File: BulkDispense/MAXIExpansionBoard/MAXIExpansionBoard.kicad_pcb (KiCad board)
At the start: 2 copper layers, 57.2 x 100 mm, 30 parts, among them J1 BS1~4, J10 FS3, J11 R6~R7, J12 R8~R9, J13 OS1~4, J14 WV1~2, J15 FS2, J16 FS4, J17 Analog Inputs, J18 Digital IN + R0~R4, J19 Digital Outputs, J2 MV1~4, J20 R4~R9, J21 Flow Sensors, J3 WB/WL, J4 PS/PCV, J5 Screw_Terminal_01x02, J6 R0~R1, J7 R2~R3, J8 R4~R5, J9 FS1

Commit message: Design Overhaul
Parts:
- removed kibuzzard-684C282C: G***, kibuzzard-684C282C
- removed kibuzzard-684C2929: G***, kibuzzard-684C2929
- removed kibuzzard-684C293C: G***, kibuzzard-684C293C
- removed kibuzzard-684C2942: G***, kibuzzard-684C2942
- removed kibuzzard-684C2947: G***, kibuzzard-684C2947
- added H10: MountingHole, MountingHole:MountingHole_2.5mm, F.Cu at (200.6, 84.4)
- added H11: MountingHole, MountingHole:MountingHole_3.2mm_M3, F.Cu at (125.2, 42.7)
- added H5: MountingHole, MountingHole:MountingHole_2.5mm, F.Cu at (213.3, 104.7)
- added H6: MountingHole, MountingHole:MountingHole_2.5mm, F.Cu at (200.6, 104.7)
- added H7: MountingHole, MountingHole:MountingHole_2.5mm, F.Cu at (213.3, 120.0)
- added H8: MountingHole, MountingHole:MountingHole_2.5mm, F.Cu at (213.3, 135.3)
- added H9: MountingHole, MountingHole:MountingHole_2.5mm, F.Cu at (213.3, 84.4)
- added J22: OS1~4, PartsLibrary:CONN_37204-62A3-004PL_3MM, F.Cu at (182.4, 76.4)
- added J23: WB-MV5~6, PartsLibrary:CONN_37204-62A3-004PL_3MM, F.Cu at (163.0, 76.5)
- H1, H2, H3, H4: footprint MountingHole:MountingHole_2.2mm_M2 -> MountingHole:MountingHole_3.2mm_M3
- J1: value BS1~4 -> R0~R5; footprint PartsLibrary:CONN_37204-62A3-004PL_3MM -> PartsLibrary:CONN_37212-62M3-003PL_3MM
- J10: value FS3 -> FS2~FS4; footprint PartsLibrary:CONN_37204-62A3-004PL_3MM -> PartsLibrary:CONN_37212-62M3-003PL_3MM
- J11: value R6~R7 -> MV1~4
- J12: value R8~R9 -> WB/WL
- J13: value OS1~4 -> PS/PCV; footprint PartsLibrary:CONN_37204-62A3-004PL_3MM -> PartsLibrary:3720362A3003PL
- J14: value WV1~2 -> RV1&2; footprint PartsLibrary:3720362A3003PL -> PartsLibrary:CONN_37204-62A3-004PL_3MM
- J15: value FS2 -> RV3&4
- J16: value FS4 -> FS1
- J17: value Analog Inputs -> FS3; footprint PartsLibrary:CONN_37212-62M3-003PL_3MM -> PartsLibrary:CONN_37204-62A3-004PL_3MM
- J18: value Digital IN + R0~R4 -> WB-MV1~4; footprint PartsLibrary:CONN_37212-62M3-003PL_3MM -> PartsLibrary:CONN_37204-62A3-004PL_3MM
- J19: value Digital Outputs -> FS2; footprint PartsLibrary:CONN_37212-62M3-003PL_3MM -> PartsLibrary:CONN_37204-62A3-004PL_3MM
- J2: value MV1~4 -> BS1~4; footprint PartsLibrary:CONN_37204-62A3-004PL_3MM -> PartsLibrary:CONN_37212-62M3-003PL_3MM
- J20: value R4~R9 -> FS4; footprint PartsLibrary:CONN_37212-62M3-003PL_3MM -> PartsLibrary:CONN_37204-62A3-004PL_3MM
- J21: value Flow Sensors -> BS1~4; footprint PartsLibrary:CONN_37212-62M3-003PL_3MM -> PartsLibrary:CONN_37204-62A3-004PL_3MM
- J3: value WB/WL -> Screw_Terminal_01x02; footprint PartsLibrary:CONN_37204-62A3-004PL_3MM -> PartsLibrary:691137710002
- J4: value PS/PCV -> DigitalOUT 0~3; footprint PartsLibrary:3720362A3003PL -> PartsLibrary:CONN_37204-62A3-004PL_3MM
- J5: value Screw_Terminal_01x02 -> DigitalOUT 4~7; footprint PartsLibrary:691137710002 -> PartsLibrary:CONN_37204-62A3-004PL_3MM
- J6: value R0~R1 -> OS1~4; footprint PartsLibrary:CONN_37204-62A3-004PL_3MM -> PartsLibrary:CONN_37212-62M3-003PL_3MM
- J7: value R2~R3 -> AnalogIOs; footprint PartsLibrary:CONN_37204-62A3-004PL_3MM -> PartsLibrary:CONN_37212-62M3-003PL_3MM
- J8: value R4~R5 -> Fan PWR; footprint PartsLibrary:CONN_37204-62A3-004PL_3MM -> PartsLibrary:3720362A3003PL
- moved J3 85.5 mm to (136.8, 47.1), turned to 180 degrees
- moved J1 79.3 mm to (130.0, 62.3), turned to 0 degrees
- moved J19 77.5 mm to (163.9, 126.7)
- moved J8 70.9 mm to (204.7, 47.1), turned to 0 degrees
- moved H1 68.1 mm to (172.8, 90.2)
- moved J6 65.3 mm to (174.6, 46.8), turned to 0 degrees
- moved J12 63.1 mm to (182.4, 69.0), turned to 0 degrees
- moved J4 57.3 mm to (130.1, 98.2), turned to 90 degrees
- moved J18 56.5 mm to (186.0, 94.8)
- moved J21 53.4 mm to (182.4, 61.6)
- moved J11 51.0 mm to (186.0, 87.3), turned to 0 degrees
- moved J5 50.9 mm to (137.7, 98.2), turned to 90 degrees
- moved H4 42.7 mm to (220.2, 137.7)
- moved H3 42.7 mm to (220.2, 42.8)
- moved J9 39.1 mm to (145.3, 98.3)
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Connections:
- J1 pad 1: /AI0 -> /R0_IN
- J1 pad 2: /AI1 -> /R1_IN
- J1 pad 3: /AI2 -> /R2_IN
- J1 pad 4: /AI3 -> /R3_IN
- J1 pad 5: (no net) -> /R4_IN
- J1 pad 6: (no net) -> /R5_IN
- J10 pad 1: /FS3-1 -> /FS2-1
- J10 pad 2: /FS3-2 -> /FS2-2
- J10 pad 3: /FS3-3 -> /FS2-3
- J10 pad 4: /FS3-4 -> /FS2-4
- J10 pad 5: (no net) -> /FS3-1
- J10 pad 6: (no net) -> /FS3-2
- J11 pad 1: /R6_OUT -> /DO0
- J11 pad 2: /R6_IN -> /DO1
- J11 pad 3: /R7_OUT -> /DO2
- J11 pad 4: /R7_IN -> /DO3
- J12 pad 1: /R8_OUT -> /AI4
- J12 pad 2: /R8_IN -> /AI5
- J12 pad 3: /R9_OUT -> /AI6
- J12 pad 4: /R9_IN -> /AI7
- J13 pad 1: /DI0 -> /AI12
- J13 pad 2: /DI1 -> /AI13
- J13 pad 3: /DI2 -> /AO0
- J14 pad 1: /AI8 -> /R0_OUT
- J14 pad 2: /AI9 -> /R0_IN
- J14 pad 3: unconnected-(J14-Pin_3-Pad3) -> /R1_OUT
- J15 pad 1: /FS2-1 -> /R2_OUT
- J15 pad 2: /FS2-2 -> /R2_IN
- J15 pad 3: /FS2-3 -> /R3_OUT
- J15 pad 4: /FS2-4 -> /R3_IN
- J16 pad 1: /FS4-1 -> /FS1-1
- J16 pad 2: /FS4-2 -> /FS1-2
- J16 pad 3: /FS4-3 -> /FS1-3
- J16 pad 4: /FS4-4 -> /FS1-4
- J17 pad 1: /AI0 -> /FS3-1
- J17 pad 2: /AI1 -> /FS3-2
- J17 pad 3: /AI2 -> /FS3-3
- J17 pad 4: /AI3 -> /FS3-4
- J17 pad 5: /AI4 -> (no net)
- J17 pad 6: /AI5 -> (no net)
- J18 pad 1: /DI0 -> /DO4
- J18 pad 2: /DI1 -> /DO5
- J18 pad 3: /DI2 -> /DO6
- J18 pad 4: /DI3 -> /DO7
- J18 pad 5: /R0_IN -> (no net)
- J18 pad 6: /R1_IN -> (no net)
- J19 pad 1: +24V -> /FS2-1
- J19 pad 2: GND -> /FS2-2
- J19 pad 3: /AI12 -> /FS2-3
- J19 pad 4: /AI13 -> /FS2-4
- J19 pad 5: /DO0 -> (no net)
- J19 pad 6: /DO1 -> (no net)
- J2 pad 1: /DO0 -> +24V
- J2 pad 2: /DO1 -> GND
- J2 pad 3: /DO2 -> /AI0
- J2 pad 4: /DO3 -> +24V
- J2 pad 5: (no net) -> GND
- J2 pad 6: (no net) -> /AI1
- J20 pad 1: /R4_IN -> /FS4-1
- J20 pad 2: /R5_IN -> /FS4-2
- J20 pad 3: /R6_IN -> /FS4-3
- J20 pad 4: /R7_IN -> /FS4-4
- J20 pad 5: /R8_IN -> (no net)
- J20 pad 6: /R9_IN -> (no net)
- J21 pad 1: /FS2-3 -> /AI0
- J21 pad 2: /FS2-4 -> /AI1
- J21 pad 3: /FS3-1 -> /AI2
- J21 pad 4: /FS3-2 -> /AI3
- J21 pad 5: /FS3-3 -> (no net)
- J21 pad 6: /FS3-4 -> (no net)
- J3 pad 1: /AI4 -> +24V
- J3 pad 2: /AI5 -> GND
- J4 pad 1: /AI12 -> /DO0
- J4 pad 2: /AI13 -> /DO1
- J4 pad 3: /AO0 -> /DO2
- J5 pad 1: +24V -> /DO4
- J5 pad 2: GND -> /DO5
- J6 pad 1: /R0_OUT -> +24V
- J6 pad 2: /R0_IN -> GND
- J6 pad 3: /R1_OUT -> /DI0
- J6 pad 4: /R1_IN -> +24V
- J6 pad 5: (no net) -> GND
- J6 pad 6: (no net) -> /DI1
- J7 pad 1: /R2_OUT -> /AI4
- J7 pad 2: /R2_IN -> /AI5
- J7 pad 3: /R3_OUT -> /AI6
- J7 pad 4: /R3_IN -> /AI7
- J7 pad 5: (no net) -> /AI12
- J7 pad 6: (no net) -> /AI13
- J8 pad 1: /R4_OUT -> +24V
- J8 pad 2: /R4_IN -> /R6_OUT
- J8 pad 3: /R5_OUT -> unconnected-(J8-Pin_3-Pad3)
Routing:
- net +24V: track 12.8 -> 132.0 mm
- net /AI8: track 84.7 -> 0.00 mm, vias 2 -> 0
- net /AI9: track 74.8 -> 0.00 mm, vias 1 -> 0
- net /AI6: track 31.8 -> 102.3 mm, vias 0 -> 1
- net /AI5: track 32.6 -> 99.9 mm, vias 0 -> 1
- net /AI4: track 32.1 -> 96.0 mm, vias 0 -> 1
- net /DO7: track 0.00 -> 58.8 mm
- net /DO5: track 0.00 -> 56.8 mm
- net /DO6: track 0.00 -> 56.6 mm
- net /FS2-4: track 31.0 -> 83.9 mm, vias 0 -> 1
- net /DO4: track 0.00 -> 50.6 mm
- net /FS2-2: track 32.3 -> 80.9 mm
- net /AI7: track 34.7 -> 81.1 mm
- net /FS2-1: track 34.3 -> 78.3 mm, vias 0 -> 1
- net /FS2-3: track 35.9 -> 79.1 mm
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- added copper zone on B.Cu, net GND
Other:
- board size 57.2 x 100 mm -> 100 x 100 mm
- board text added: "I2C Bus"
- board text added: "I2C Hot Swap"

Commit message: Add latest design
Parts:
- added H10: MountingHole, MountingHole:MountingHole_2.5mm, F.Cu at (223.5, 85.1)
- added H5: MountingHole, MountingHole:MountingHole_2.5mm, F.Cu at (210.8, 64.7)
- added H6: MountingHole, MountingHole:MountingHole_2.5mm, F.Cu at (223.5, 64.7)
- added H9: MountingHole, MountingHole:MountingHole_2.5mm, F.Cu at (210.8, 85.1)
- added J24: LDS, PartsLibrary:CONN_37204-62A3-004PL_3MM, F.Cu at (187.4, 77.7)
- J13, J8: footprint PartsLibrary:3720362A3003PL -> PartsLibrary:CONN_37203-62A3-003PL_3MM
- moved H13 57.1 mm to (257.7, 84.7), turned to 90 degrees
- moved H15 46.3 mm to (257.7, 97.4), turned to 90 degrees
- moved H12 41.8 mm to (237.3, 84.7), turned to 90 degrees
- moved H3 38.9 mm to (259.1, 43.9)
- moved H4 38.8 mm to (259.0, 136.8)
- moved H8 37.0 mm to (225.0, 100.3), turned to -90 degrees
- moved J23 35.3 mm to (187.5, 101.9)
- moved H1 30.8 mm to (203.6, 91.2)
- moved H14 25.1 mm to (237.3, 97.4), turned to 90 degrees
- moved J19 25.1 mm to (187.4, 118.0)
- moved J17 24.6 mm to (187.4, 126.0)
- moved J16 23.7 mm to (187.4, 109.9)
- moved J20 23.5 mm to (187.4, 134.1)
- moved J11 21.6 mm to (166.5, 77.9)
- moved H7 20.1 mm to (209.6, 100.2), turned to -90 degrees
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- renumbered H6 to H12, H10 to H13, H5 to H14, H9 to H15
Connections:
- J7 pad 10: +24V -> /LDS
- J7 pad 11: unconnected-(J7-Pin_11-Pad11) -> +24V
- J7 pad 7: unconnected-(J7-Pin_7-Pad7) -> /AO0
- J7 pad 8: /AO0 -> /LDS-5V
- J7 pad 9: unconnected-(J7-Pin_9-Pad9) -> /LDS-GND
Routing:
- net GND: track 0.00 -> 122.6 mm
- net +24V: track 132.0 -> 220.9 mm
- net /LDS: track 0.00 -> 79.4 mm, vias 0 -> 1
- net /LDS-GND: track 0.00 -> 76.9 mm, vias 0 -> 1
- net /LDS-5V: track 0.00 -> 71.0 mm, vias 0 -> 1
- net /R4_OUT: track 18.5 -> 67.4 mm, vias 0 -> 1
- net /R4_IN: track 36.7 -> 80.0 mm
- net /R5_OUT: track 25.6 -> 67.2 mm
- net /R5_IN: track 39.0 -> 76.1 mm
- net /FS4-1: track 61.7 -> 88.9 mm, vias 0 -> 1
- net /FS3-4: track 61.6 -> 85.8 mm
- net /AI12: track 32.4 -> 54.9 mm, vias 0 -> 1
- net /FS3-1: track 62.5 -> 84.1 mm
- net /FS4-2: track 63.7 -> 84.6 mm, vias 0 -> 1
- net /AI5: track 99.9 -> 82.4 mm
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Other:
- board size 100 x 100 mm -> 139.7 x 100 mm
- board text added: "BS1 BS2"
- board text added: "BS1~4"
- board text added: "BS3 BS4"
- board text added: "FS1"
- board text added: "FS2"
- board text added: "FS3"
- board text added: "FS4"
- board text added: "Fan PWR"
- board text added: "LEAK"
- board text added: "MV1 MV2"
- board text added: "MV3 MV4"
- board text added: "MV5 MV6"
- board text added: "OS1 OS2"
- board text added: "OS1~4"
- board text added: "OS3 OS4"
- board text added: "PORT1 R0~R5"
- board text added: "PORT2 FS2~ FS4"
- board text added: "PORT3 DO FS1"
- board text added: "PORT4 AIO"
- board text added: "PS PCV"
- board text added: "RV1 RV2"
- board text added: "RV3 RV4"
- board text added: "Temp/Humidity Sensor"
- board text added: "WB"
- board text added: "WB MV1~4"
- board text added: "WB WL"

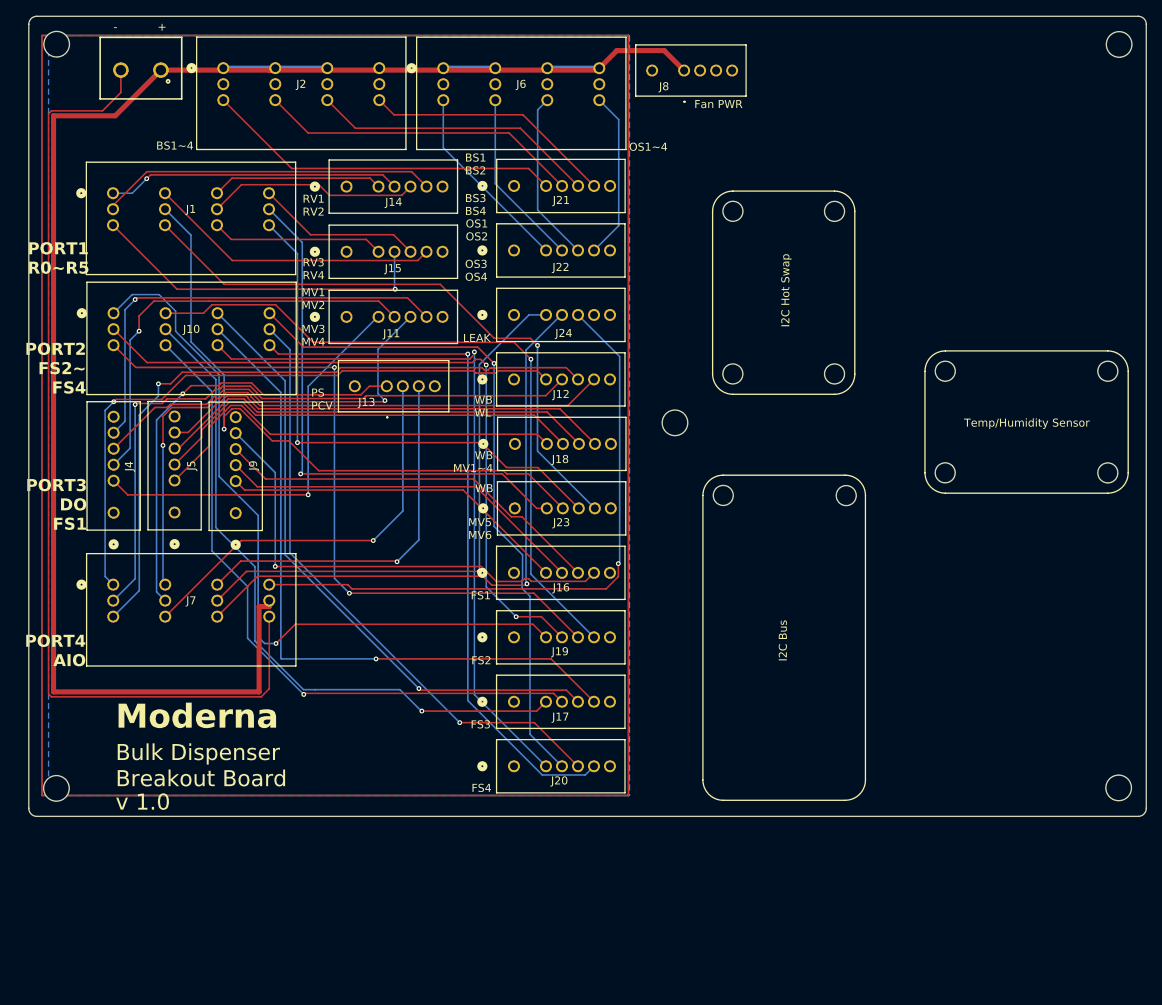
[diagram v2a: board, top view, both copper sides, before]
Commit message: Update PCB + Add Lynx Wiring Diagram
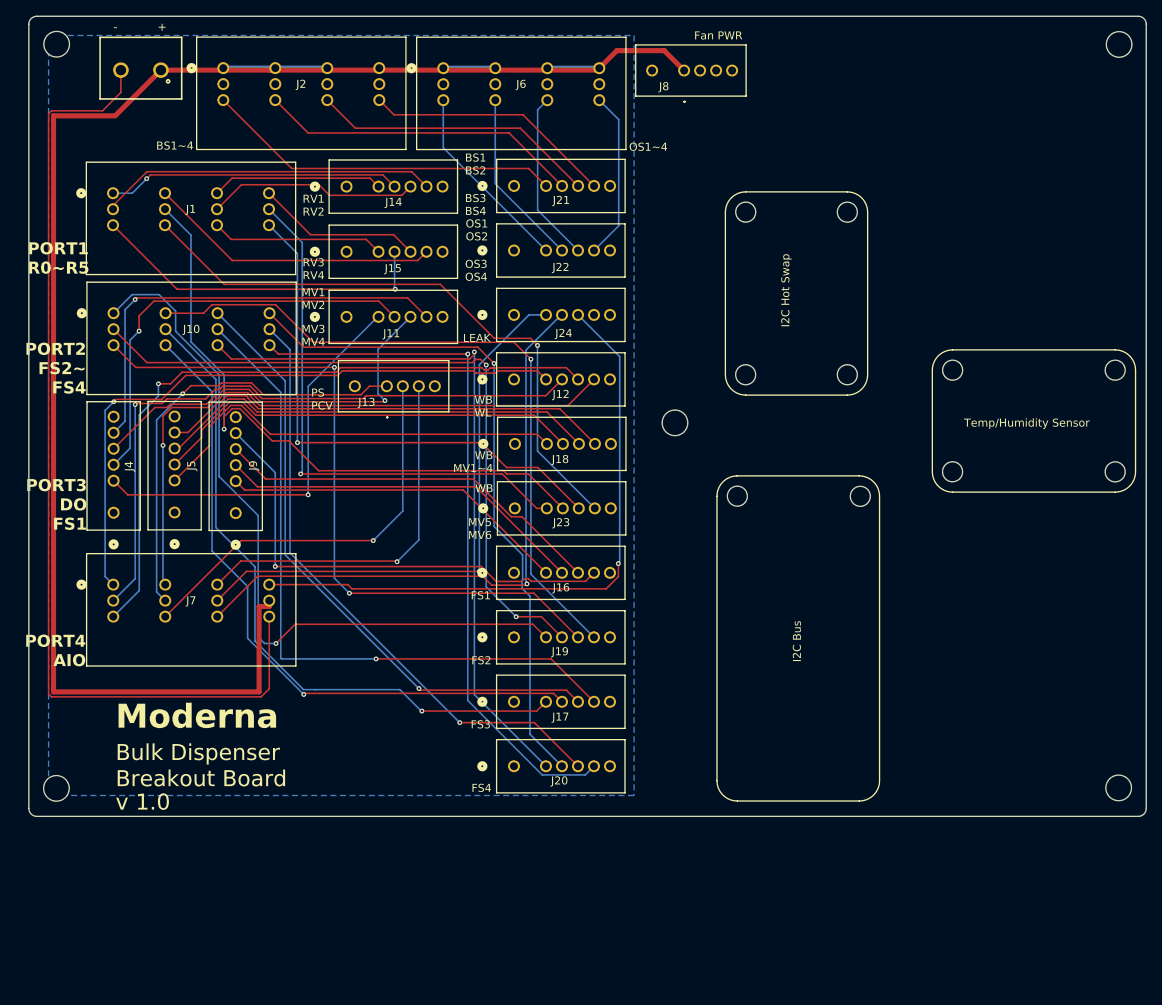
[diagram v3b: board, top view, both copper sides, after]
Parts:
- moved H8 1.76 mm to (226.7, 100.4)
- moved H7 1.76 mm to (211.3, 100.3)
- moved H9 1.60 mm to (212.4, 85.2)
- moved H6 1.60 mm to (225.1, 64.8)
- moved H10 1.60 mm to (225.1, 85.2)
- moved H5 1.60 mm to (212.4, 64.8)
- moved H15 0.93 mm to (258.6, 97.3)
- moved H12 0.93 mm to (238.3, 84.6)
- moved H13 0.93 mm to (258.6, 84.6)
- moved H14 0.93 mm to (238.2, 97.3)
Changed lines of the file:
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@@
 	(footprint "MountingHole:MountingHole_2.5mm"
 		(layer "F.Cu")
-		(at 223.4939 85.0561)
+		(at 225.0939 85.1561)
 		(descr "Mounting Hole 2.5mm, no annular, generated by kicad-footprint-generator mountinghole.py")
 		(tags "mountinghole")
@@
 	(footprint "MountingHole:MountingHole_2.5mm"
 		(layer "F.Cu")
-		(at 257.6561 84.7161 90)
+		(at 258.5761 84.5861 90)
 		(descr "Mounting Hole 2.5mm, no annular, generated by kicad-footprint-generator mountinghole.py")
 		(tags "mountinghole")
@@
 	(footprint "MountingHole:MountingHole_2.5mm"
 		(layer "F.Cu")
-		(at 223.4939 64.7361)
+		(at 225.0939 64.8361)
 		(descr "Mounting Hole 2.5mm, no annular, generated by kicad-footprint-generator mountinghole.py")
 		(tags "mountinghole")
@@
 	(footprint "MountingHole:MountingHole_2.5mm"
 		(layer "F.Cu")
-		(at 210.7939 64.7261)
+		(at 212.3939 64.8261)
 		(descr "Mounting Hole 2.5mm, no annular, generated by kicad-footprint-generator mountinghole.py")
 		(tags "mountinghole")
@@
 	(footprint "MountingHole:MountingHole_2.5mm"
 		(layer "F.Cu")
-		(at 224.956 100.264 -90)
+		(at 226.716 100.354 -90)
 		(descr "Mounting Hole 2.5mm, no annular, generated by kicad-footprint-generator mountinghole.py")
 		(tags "mountinghole")
@@
 	(footprint "MountingHole:MountingHole_2.5mm"
 		(layer "F.Cu")
-		(at 257.6561 97.4261 90)
+		(at 258.5761 97.2961 90)
 		(descr "Mounting Hole 2.5mm, no annular, generated by kicad-footprint-generator mountinghole.py")
 		(tags "mountinghole")
@@
 	(footprint "MountingHole:MountingHole_2.5mm"
 		(layer "F.Cu")
-		(at 209.586 100.244 -90)
+		(at 211.346 100.334 -90)
 		(descr "Mounting Hole 2.5mm, no annular, generated by kicad-footprint-generator mountinghole.py")
 		(tags "mountinghole")
@@
 	(footprint "MountingHole:MountingHole_2.5mm"
 		(layer "F.Cu")
-		(at 237.3361 84.7161 90)
+		(at 238.2561 84.5861 90)
 		(descr "Mounting Hole 2.5mm, no annular, generated by kicad-footprint-generator mountinghole.py")
 		(tags "mountinghole")
@@
 	(footprint "MountingHole:MountingHole_2.5mm"
 		(layer "F.Cu")
-		(at 237.3261 97.4161 90)
+		(at 238.2461 97.2861 90)
 		(descr "Mounting Hole 2.5mm, no annular, generated by kicad-footprint-generator mountinghole.py")
 		(tags "mountinghole")
@@
 	(footprint "MountingHole:MountingHole_2.5mm"
 		(layer "F.Cu")
-		(at 210.7839 85.0561)
+		(at 212.3839 85.1561)
 		(descr "Mounting Hole 2.5mm, no annular, generated by kicad-footprint-generator mountinghole.py")
 		(tags "mountinghole")
@@
 		(embedded_fonts no)
 	)
-	(gr_rect
-		(start 124.43 42.75)
-		(end 197.74 137.75)
-		(stroke
-			(width 0.2)
-			(type solid)
-		)
-		(fill no)
-		(layer "F.Cu")
-		(net 3)
-	)
-	(gr_rect
-		(start 124.43 42.75)
-		(end 197.74 137.75)
-		(stroke
-			(width 0.2)
-			(type solid)
-		)
-		(fill no)
-		(layer "B.Cu")
-	)
 	(gr_line
-		(start 237.34 99.96)
-		(end 257.66 99.96)
+		(start 238.26 99.83)
+		(end 258.58 99.83)
 		(stroke
 			(width 0.05)
@@
 	)
 	(gr_line
-		(start 223.49 62.2)
-		(end 210.79 62.2)
+		(start 225.09 62.3)
+		(end 212.39 62.3)
 		(stroke
 			(width 0.05)
@@
 	)
 	(gr_line
-		(start 234.8 84.72)
-		(end 234.8 97.42)
+		(start 235.72 84.59)
+		(end 235.72 97.29)
 		(stroke
 			(width 0.05)
@@
 	)
 	(gr_arc
-		(start 207.04 100.25)
-		(mid 207.783952 98.453966)
-		(end 209.58 97.71)
+		(start 208.8 100.34)
+		(mid 209.543952 98.543966)
+		(end 211.34 97.8)
 		(stroke
 			(width 0.05)
@@
 	)
 	(gr_arc
-		(start 237.34 99.96)
-		(mid 235.543949 99.216051)
-		(end 234.8 97.42)
+		(start 238.26 99.83)
+		(mid 236.463949 99.086051)
+		(end 235.72 97.29)
 		(stroke
 			(width 0.05)
@@
 	)
 	(gr_line
-		(start 208.25 64.74)
-		(end 208.25 85.06)
+		(start 209.85 64.84)
+		(end 209.85 85.16)
 		(stroke
 			(width 0.05)
@@
 	)
 	(gr_arc
-		(start 224.82 97.71)
-		(mid 226.61602 98.453966)
-		(end 227.36 100.25)
+		(start 226.58 97.8)
+		(mid 228.37602 98.543966)
+		(end 229.12 100.34)
 		(stroke
 			(width 0.05)
@@
 	)
 	(gr_line
-		(start 257.66 82.18)
-		(end 237.34 82.18)
+		(start 258.58 82.05)
+		(end 238.26 82.05)
 		(stroke
 			(width 0.05)
@@
 	)
 	(gr_line
-		(start 227.36 135.81)
-		(end 227.36 100.25)
+		(start 229.12 135.9)
+		(end 229.12 100.34)
 		(stroke
 			(width 0.05)
@@
 	)
 	(gr_arc
-		(start 223.49 62.2)
-		(mid 225.286051 62.943949)
-		(end 226.03 64.74)
+		(start 225.09 62.3)
+		(mid 226.886051 63.043949)
+		(end 227.63 64.84)
 		(stroke
 			(width 0.05)
@@
 	)
 	(gr_arc
-		(start 210.79 87.6)
-		(mid 208.993949 86.856051)
-		(end 208.25 85.06)
+		(start 212.39 87.7)
+		(mid 210.593949 86.956051)
+		(end 209.85 85.16)
 		(stroke
 			(width 0.05)
@@
 	)
 	(gr_arc
-		(start 227.36 135.81)
-		(mid 226.616054 137.606068)
-		(end 224.82 138.35)
+		(start 229.12 135.9)
+		(mid 228.376054 137.696068)
+		(end 226.58 138.44)
 		(stroke
 			(width 0.05)
@@
 	)
 	(gr_arc
-		(start 226.03 85.06)
-		(mid 225.286052 86.856052)
-		(end 223.49 87.6)
+		(start 227.63 85.16)
+		(mid 226.886052 86.956052)
+		(end 225.09 87.7)
 		(stroke
 			(width 0.05)
@@
 	)
 	(gr_arc
-		(start 257.66 82.18)
-		(mid 259.456051 82.923949)
-		(end 260.2 84.72)
+		(start 258.58 82.05)
+		(mid 260.376051 82.793949)
+		(end 261.12 84.59)
 		(stroke
 			(width 0.05)
@@
 	)
 	(gr_line
-		(start 207.04 100.25)
-		(end 207.04 135.81)
+		(start 208.8 100.34)
+		(end 208.8 135.9)
 		(stroke
 			(width 0.05)
@@
 	)
 	(gr_line
-		(start 260.2 97.42)
-		(end 260.2 84.72)
+		(start 261.12 97.29)
+		(end 261.12 84.59)
 		(stroke
 			(width 0.05)
@@
 	)
 	(gr_line
-		(start 226.03 85.06)
-		(end 226.03 64.74)
+		(start 227.63 85.16)
+		(end 227.63 64.84)
 		(stroke
 			(width 0.05)
@@
 	)
 	(gr_arc
-		(start 260.2 97.42)
-		(mid 259.456051 99.216051)
-		(end 257.66 99.96)
+		(start 261.12 97.29)
+		(mid 260.376051 99.086051)
+		(end 258.58 99.83)
 		(stroke
 			(width 0.05)
@@
 	)
 	(gr_arc
-		(start 208.25 64.74)
-		(mid 208.993949 62.943948)
-		(end 210.79 62.2)
+		(start 209.85 64.84)
+		(mid 210.593949 63.043948)
+		(end 212.39 62.3)
 		(stroke
 			(width 0.05)
@@
 	)
 	(gr_arc
-		(start 234.8 84.72)
-		(mid 235.543949 82.923949)
-		(end 237.34 82.18)
+		(start 235.72 84.59)
+		(mid 236.463949 82.793949)
+		(end 238.26 82.05)
 		(stroke
 			(width 0.05)
@@
 	)
 	(gr_arc
-		(start 209.58 138.35)
-		(mid 207.783918 137.606068)
-		(end 207.04 135.81)
+		(start 211.34 138.44)
+		(mid 209.543918 137.696068)
+		(end 208.8 135.9)
 		(stroke
 			(width 0.05)
@@
 	)
 	(gr_line
-		(start 209.58 138.35)
-		(end 224.82 138.35)
+		(start 211.34 138.44)
+		(end 226.58 138.44)
 		(stroke
 			(width 0.05)
@@
 	)
 	(gr_line
-		(start 210.79 87.6)
-		(end 223.49 87.6)
+		(start 212.39 87.7)
+		(end 225.09 87.7)
 		(stroke
 			(width 0.05)
@@
 	)
 	(gr_line
-		(start 224.8 97.71)
-		(end 209.56 97.71)
+		(start 226.56 97.8)
+		(end 211.32 97.8)
 		(stroke
 			(width 0.05)
@@
 	)
 	(gr_text "I2C Bus"
-		(at 217.066051 118.393949 90)
+		(at 218.826051 118.483949 90)
 		(layer "F.SilkS")
 		(effects
@@
 	)
 	(gr_text "Fan PWR"
-		(at 205.95 51.94 0)
+		(at 205.93 43.36 0)
 		(layer "F.SilkS")
 		(effects
@@
 	)
 	(segment
-		(start 149.9906 109.7367)
-		(end 146.3334 113.3939)
+		(start 179.1045 109.7367)
+		(end 149.9906 109.7367)
 		(width 0.2)
 		(layer "F.Cu")
@@
 	)
 	(segment
-		(start 179.1045 109.7367)
-		(end 149.9906 109.7367)
+		(start 149.9906 109.7367)
+		(end 146.3334 113.3939)
 		(width 0.2)
 		(layer "F.Cu")
@@
 	)
 	(segment
-		(start 185.3009 77.68)
-		(end 179.1045 83.8764)
+		(start 179.1045 83.8764)
+		(end 185.3009 77.68)
 		(width 0.2)
 		(layer "B.Cu")
@@
 	)
 	(segment
-		(start 179.1045 83.8764)
-		(end 179.1045 109.7367)
+		(start 179.1045 109.7367)
+		(end 179.1045 83.8764)
 		(width 0.2)
 		(layer "B.Cu")
@@
 	)
 	(segment
-		(start 187.43 77.68)
-		(end 185.3009 77.68)
+		(start 185.3009 77.68)
+		(end 187.43 77.68)
 		(width 0.2)
 		(layer "B.Cu")
@@
 		(polygon
 			(pts
-				(xy 125.25 42.75) (xy 197.87 42.75) (xy 197.87 137.75) (xy 125.25 137.75)
+				(xy 125.25 42.75) (xy 198.43 42.75) (xy 198.43 137.75) (xy 125.25 137.75)
 			)
 		)

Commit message: Add updated layout
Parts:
- J13, J8: footprint PartsLibrary:CONN_37203-62A3-003PL_3MM -> PartsLibrary:CONN_37204-62A3-004PL_3MM
- moved J8 2.79 mm to (207.4, 47.5)
- moved J13 0.99 mm to (166.6, 86.9)
- renumbered H13 to H10, H14 to H5, H12 to H6, H15 to H9
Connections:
- J8 pad 2: /R6_OUT -> unconnected-(J8-Pin_2-Pad2)
- J8 pad 3: unconnected-(J8-Pin_3-Pad3) -> /R6_OUT
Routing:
- net +24V: track 220.9 -> 196.9 mm
- net /DO2: track 50.5 -> 48.8 mm
- net /DO0: track 51.0 -> 52.5 mm
- net /FS2-3: track 88.6 -> 87.2 mm
- net /AI12: track 54.9 -> 53.8 mm
- net /R2_IN: track 43.3 -> 42.5 mm
